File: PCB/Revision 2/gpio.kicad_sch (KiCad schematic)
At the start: 1 part, among them J3 Conn_02x10_Odd_Even

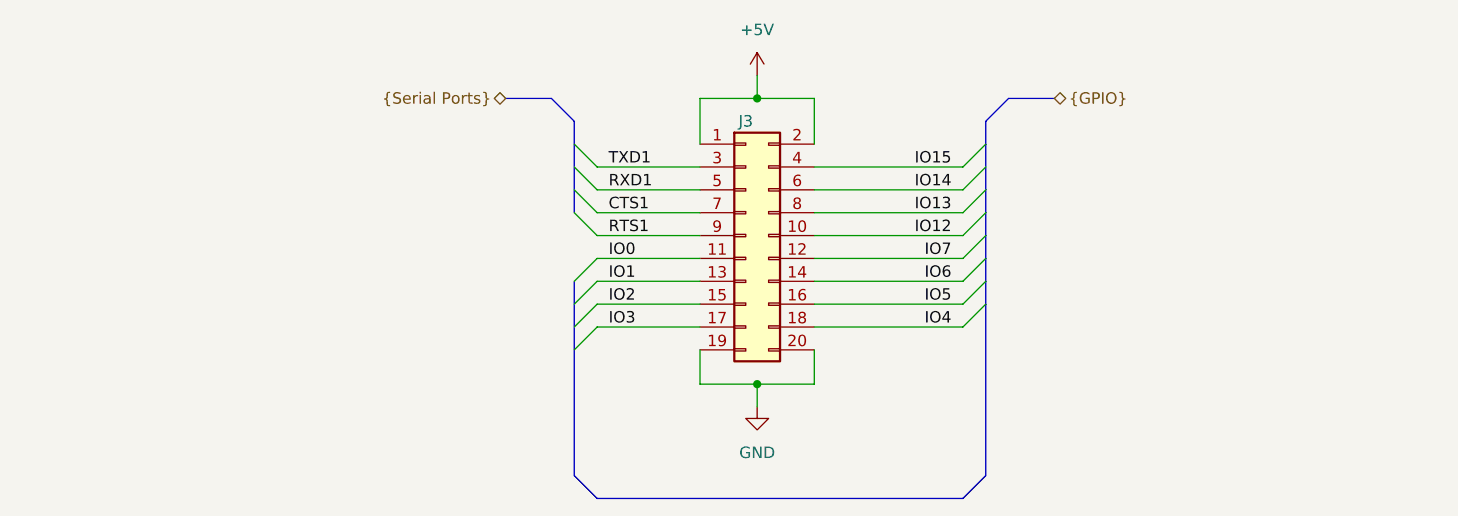
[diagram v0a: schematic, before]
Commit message: ESD protection diodes go BRRRRRRR
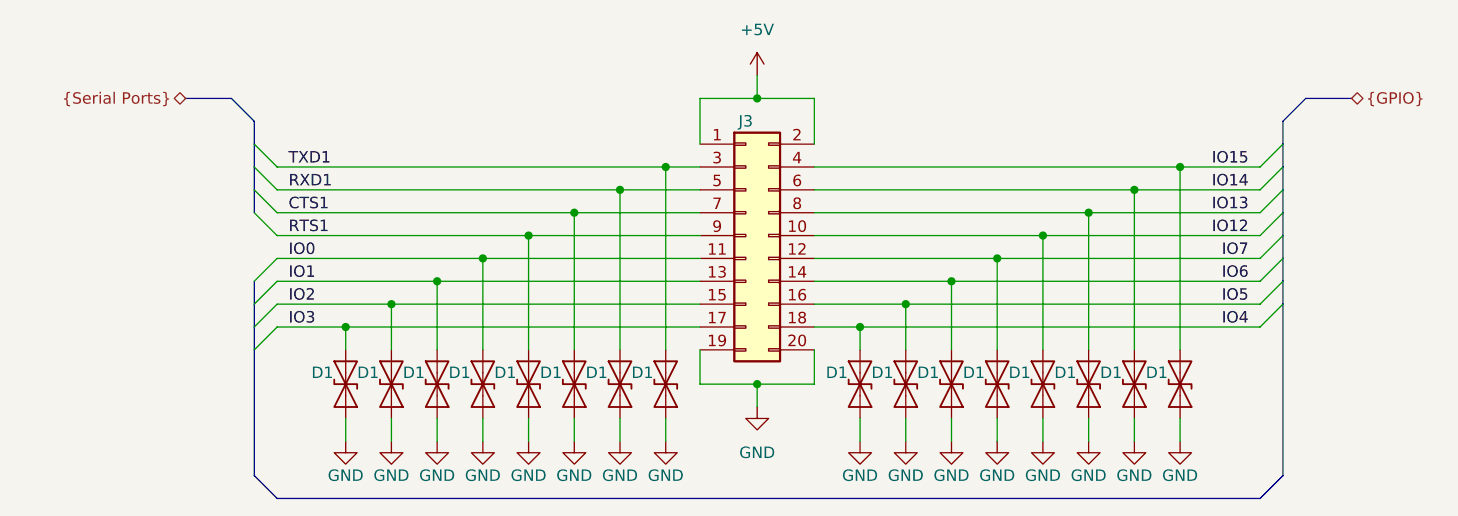
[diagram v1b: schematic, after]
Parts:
- added D1 (x16): ESD9B3.3ST5G, Diode_SMD:D_SOD-923, symbol Diode:ESD9B3.3ST5G
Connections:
- net CTS1: now also D1.1 (A1)
- net GND: now also D1.2 (A2), D1.2 (A2), D1.2 (A2), D1.2 (A2), D1.2 (A2), D1.2 (A2), D1.2 (A2), D1.2 (A2), D1.2 (A2), D1.2 (A2), D1.2 (A2), D1.2 (A2), D1.2 (A2), D1.2 (A2), D1.2 (A2), D1.2 (A2)
- net IO0: now also D1.1 (A1)
- net IO1: now also D1.1 (A1)
- net IO12: now also D1.1 (A1)
- net IO13: now also D1.1 (A1)
- net IO14: now also D1.1 (A1)
- net IO15: now also D1.1 (A1)
- net IO2: now also D1.1 (A1)
- net IO3: now also D1.1 (A1)
- net IO4: now also D1.1 (A1)
- net IO5: now also D1.1 (A1)
- net IO6: now also D1.1 (A1)
- net IO7: now also D1.1 (A1)
- net RTS1: now also D1.1 (A1)
- net RXD1: now also D1.1 (A1)
- net TXD1: now also D1.1 (A1)
